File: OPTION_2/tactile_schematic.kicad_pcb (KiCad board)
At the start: 2 copper layers, 109.6 x 67.4 mm, 59 parts, among them IC1 CY8C4145PVI-PS431, J1 Conn_01x02, J2 Conn_01x04, J3 Conn_01x04, J4 Conn_01x02, J5 Conn_ARM_SWD_TagConnect_TC203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

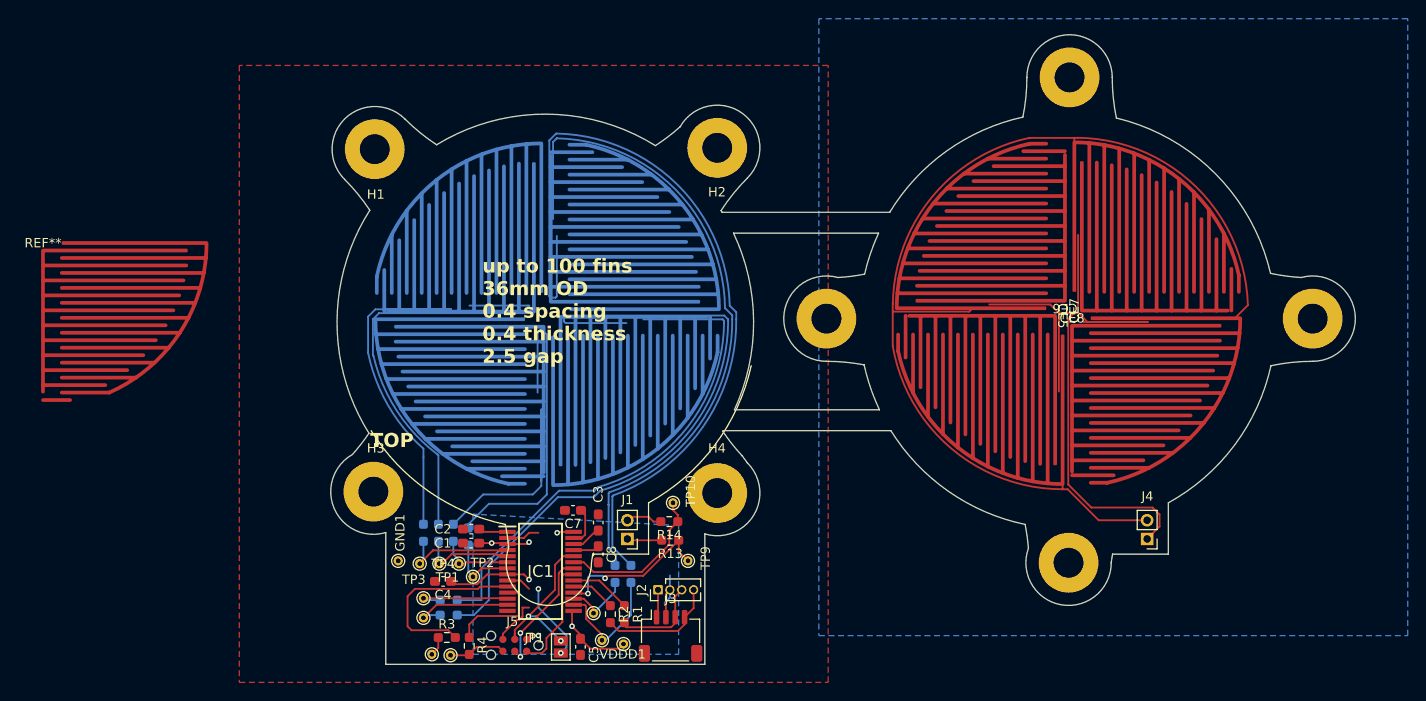
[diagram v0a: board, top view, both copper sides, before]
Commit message: three pcb trace configurations
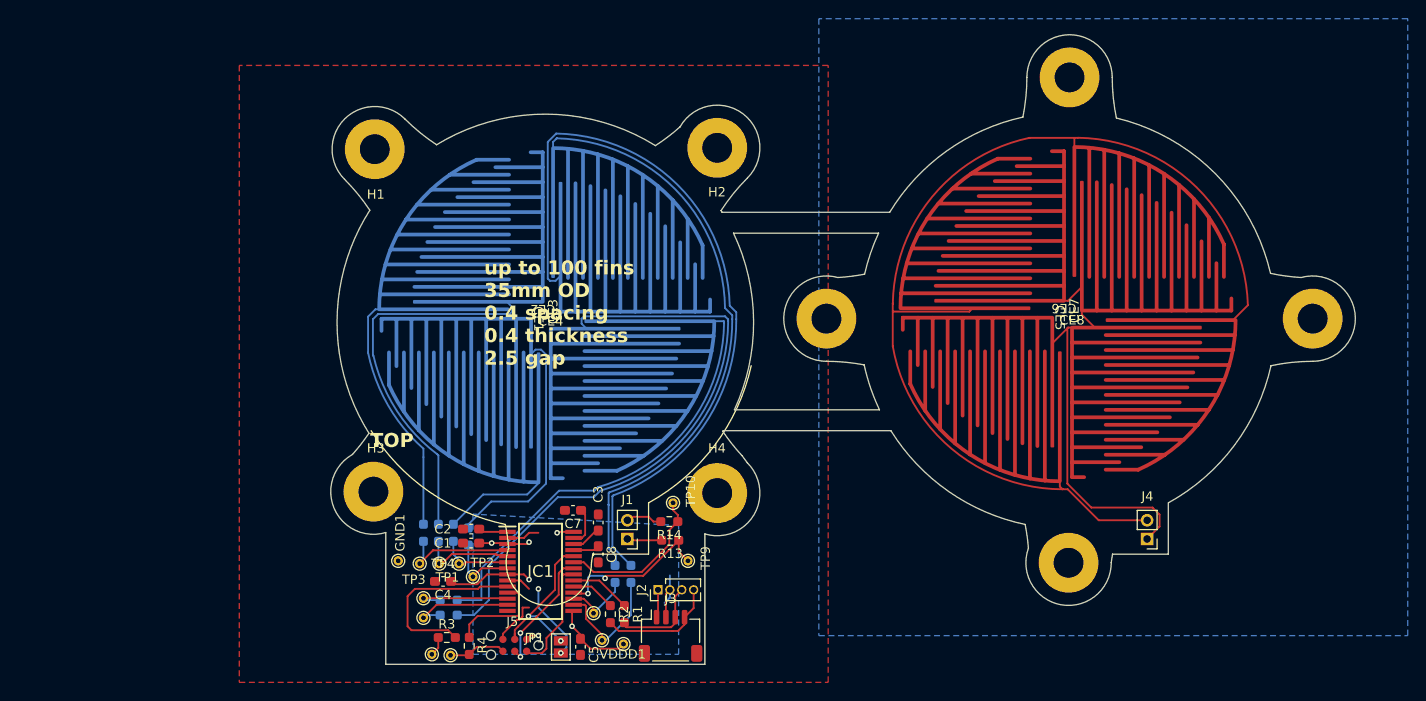
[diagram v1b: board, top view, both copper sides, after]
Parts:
- removed REF**: COIL_GENERATOR, COIL_GENERATOR
- CE1, CE2, CE3, CE4: footprint ECE382N:COIL_GENERATOR -> ECE382N:04W_04S_COIL_BACK; moved to F.Cu
- CE5, CE6, CE7, CE8: footprint ECE382N:COIL_GENERATOR -> ECE382N:04W_04S_COIL_FRONT
- moved CE4 1.28 mm to (187.3, 51.4)
- moved CE2 1.07 mm to (186.5, 50.1)
- moved CE1 0.82 mm to (186.0, 51.1), turned to -90 degrees
- moved CE3 0.56 mm to (187.6, 50.3), turned to 90 degrees
- moved CE5 0.36 mm to (241.8, 51.0)
- moved CE8 0.20 mm to (243.1, 51.2)
- moved CE6 0.10 mm to (242.2, 50.0)
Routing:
- net Net-(CE1-Pad2): track 27.0 -> 18.2 mm
- net Net-(J1-Pin_1): track 77.9 -> 84.9 mm
- net Net-(CE1-Pad1): track 34.6 -> 28.8 mm
- net Net-(CE4-Pad1): track 48.1 -> 43.2 mm
- net Net-(CE2-Pad1): track 35.8 -> 34.7 mm
- net Net-(J1-Pin_2): track 59.5 -> 58.8 mm
- net Net-(CE4-Pad2): track 31.0 -> 30.5 mm
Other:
- board text added: "up to 100 fins 35mm OD 0.4 spacing 0.4 thickness 2.5 gap"
- board text removed: "up to 100 fins 36mm OD 0.4 spacing 0.4 thickness 2.5 gap"
